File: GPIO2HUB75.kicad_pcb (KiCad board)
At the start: 2 copper layers, 33 x 57.1 mm, 3 parts, among them J1 Conn_02x10_Odd_Even, J2 Conn_02x20_Odd_Even_MountingP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, J3 Conn_02x08_Top_Bottom

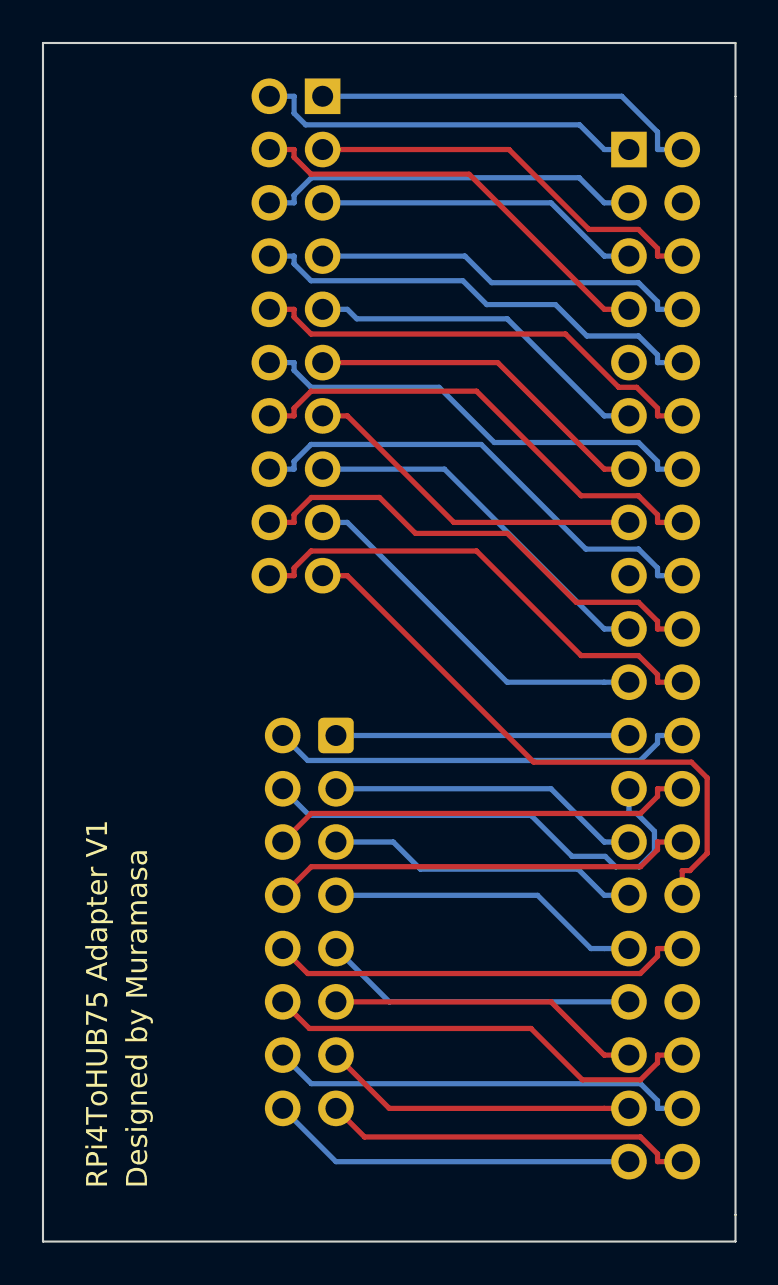
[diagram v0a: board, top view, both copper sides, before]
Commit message: added solder bridge to support 64x64+ panels
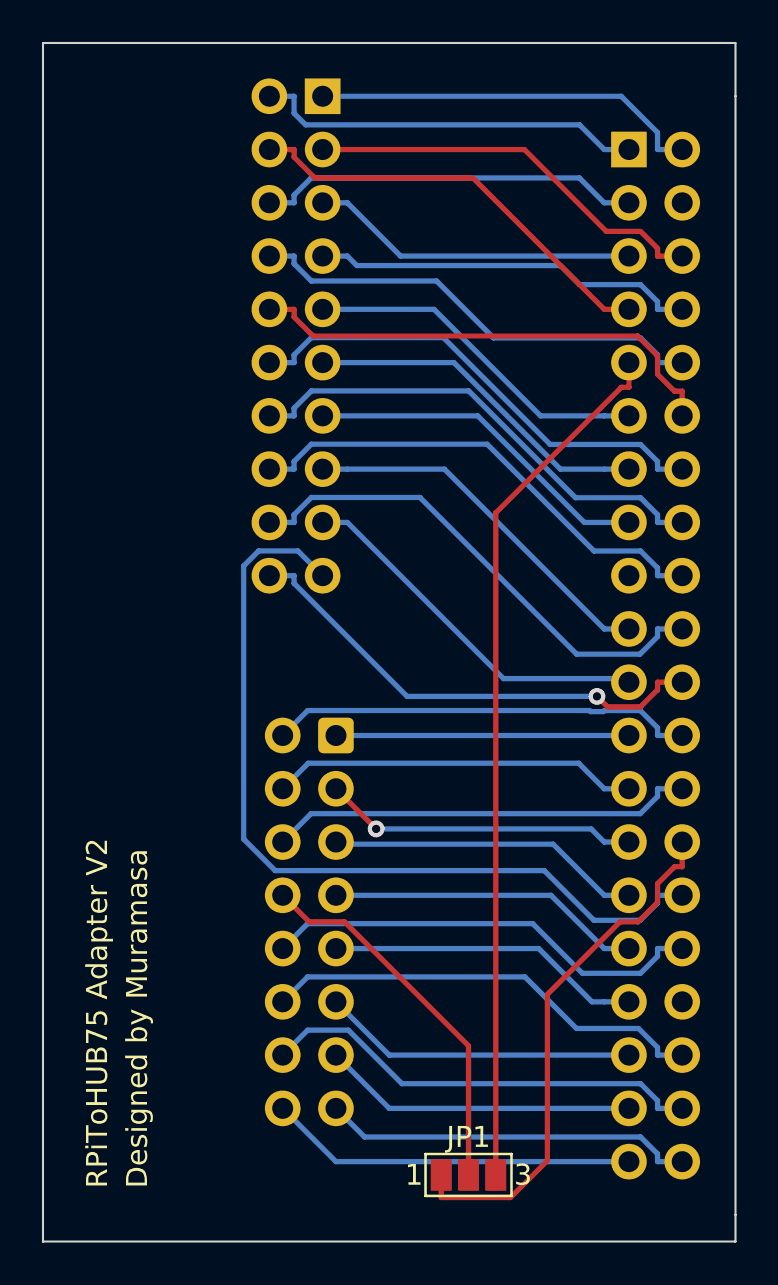
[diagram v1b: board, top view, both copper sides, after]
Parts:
- added JP1: SolderJumper_3_Open, Jumper:SolderJumper-3_P1.3mm_Open_Pad1.0x1.5mm_NumberLabels, F.Cu at (114.3, 102.2)
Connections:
- J2 pad 9: unconnected-(J2-Pin_9-Pad9) -> Net-(J2-Pin_9)
- J3 pad 8: Net-(J2-Pin_28) -> Net-(J3-Pin_8)
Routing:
- net Net-(J2-Pin_9): track 0.00 -> 41.6 mm
- net Net-(J3-Pin_8): track 0.00 -> 18.0 mm
- net Net-(J1-Pin_19): track 28.6 -> 40.8 mm
- net Net-(J2-Pin_25): track 23.3 -> 17.5 mm
- net Net-(J2-Pin_28): track 20.3 -> 25.4 mm
- net Net-(J1-Pin_18): track 23.2 -> 24.2 mm
- net Net-(J1-Pin_12): track 22.2 -> 23.2 mm
- net Net-(J2-Pin_38): track 20.3 -> 21.3 mm
- net Net-(J1-Pin_10): track 22.2 -> 23.2 mm
- net Net-(J2-Pin_32): track 20.3 -> 21.2 mm
- net Net-(J1-Pin_20): vias 0 -> 1
- net Net-(J2-Pin_27): vias 0 -> 1
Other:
- board text added: "RPiToHUB75 Adapter V2"
- board text removed: "RPi4ToHUB75 Adapter V1"

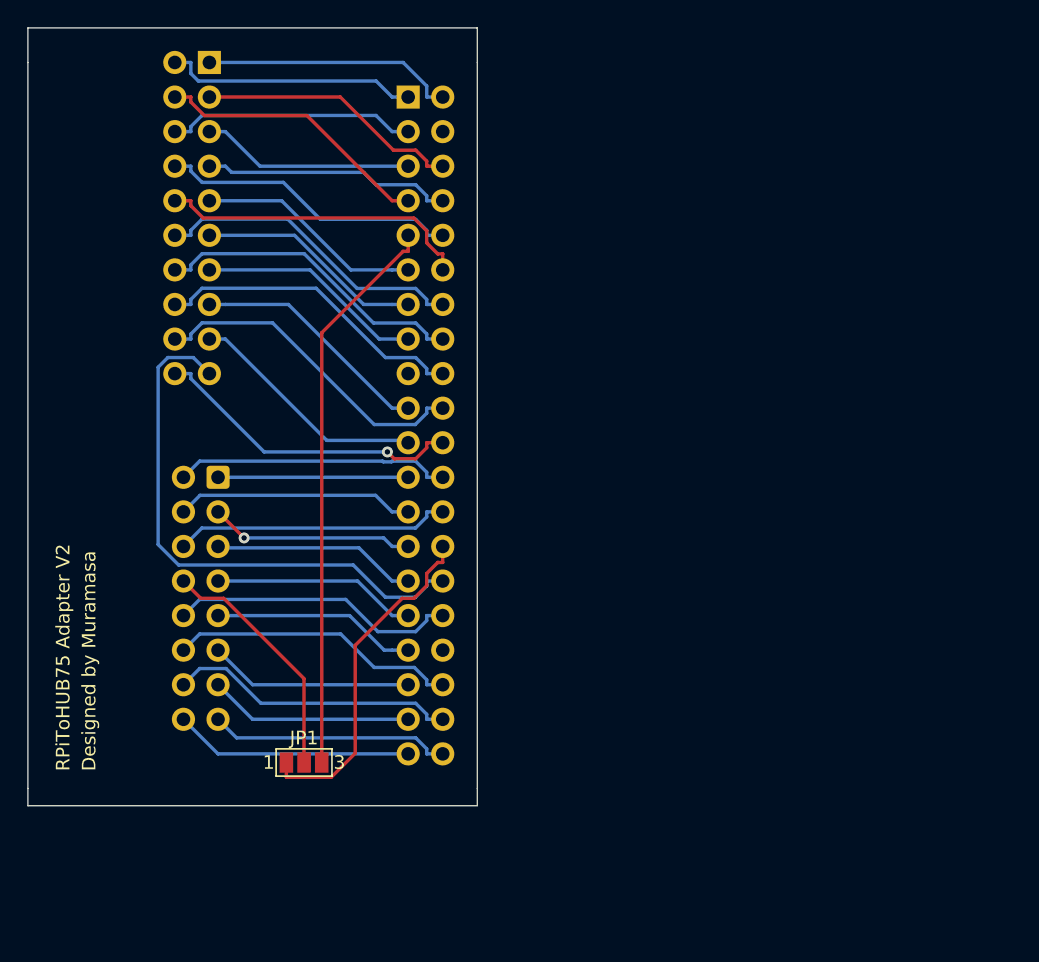
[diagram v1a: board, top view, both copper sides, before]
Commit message: added a 3pin fan header
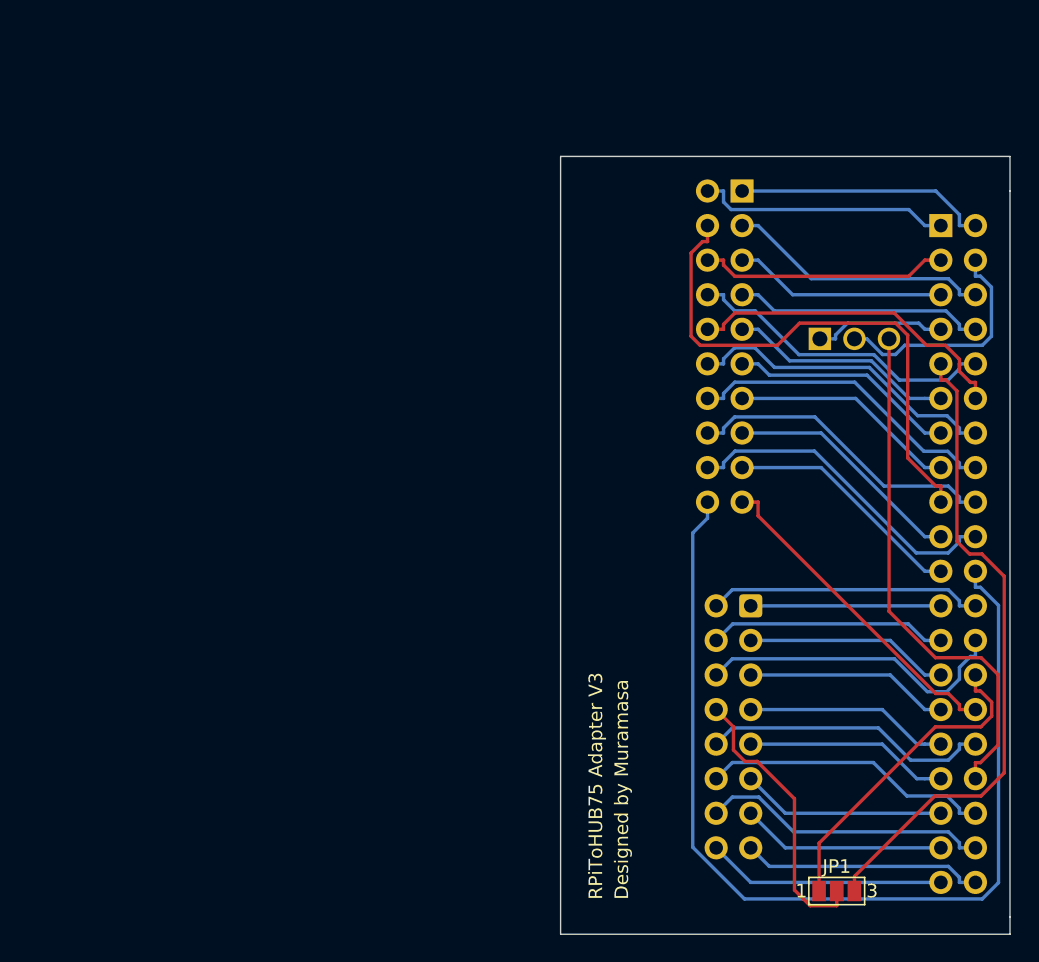
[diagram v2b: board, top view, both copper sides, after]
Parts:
- added M1: Fan_3pin, 3 Pin Fan Header Angled:HDRRA3W64P0X254_1X3_747X318X635P, B.Cu at (152.2, 71.1)
- moved J1 40.3 mm to (146.5, 60.2)
- moved J2 40.3 mm to (161.1, 62.8)
- moved J3 40.3 mm to (147.1, 90.7)
- moved JP1 40.3 mm to (153.4, 111.7)
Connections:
- J2 pad 17: unconnected-(J2-Pin_17-Pad17) -> Net-(J1-Pin_4)
- J2 pad 34: unconnected-(J2-Pin_34-Pad34) -> Net-(J2-Pin_34)
- J2 pad 4: unconnected-(J2-Pin_4-Pad4) -> Net-(J2-Pin_4)
- J2 pad 7: Net-(J1-Pin_4) -> Net-(J2-Pin_7)
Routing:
- net Net-(J1-Pin_20): track 23.2 -> 74.1 mm, vias 1 -> 0
- net Net-(J2-Pin_34): track 0.00 -> 38.5 mm
- net Net-(J1-Pin_4): track 20.5 -> 39.6 mm
- net Net-(J2-Pin_4): track 0.00 -> 17.4 mm
- net Net-(J1-Pin_19): track 40.8 -> 24.3 mm
- net Net-(J2-Pin_7): track 0.00 -> 9.72 mm
- net Net-(J2-Pin_9): track 41.6 -> 48.0 mm
- net Net-(J2-Pin_26): track 20.3 -> 23.3 mm
- net Net-(J3-Pin_8): track 18.0 -> 20.8 mm
- net Net-(J2-Pin_28): track 25.4 -> 23.8 mm
- net Net-(J1-Pin_10): track 23.2 -> 24.2 mm
- net Net-(J1-Pin_8): track 22.2 -> 23.2 mm
- net Net-(J2-Pin_27): vias 1 -> 0
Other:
- board text added: "RPiToHUB75 Adapter V3"
- board text removed: "RPiToHUB75 Adapter V2"

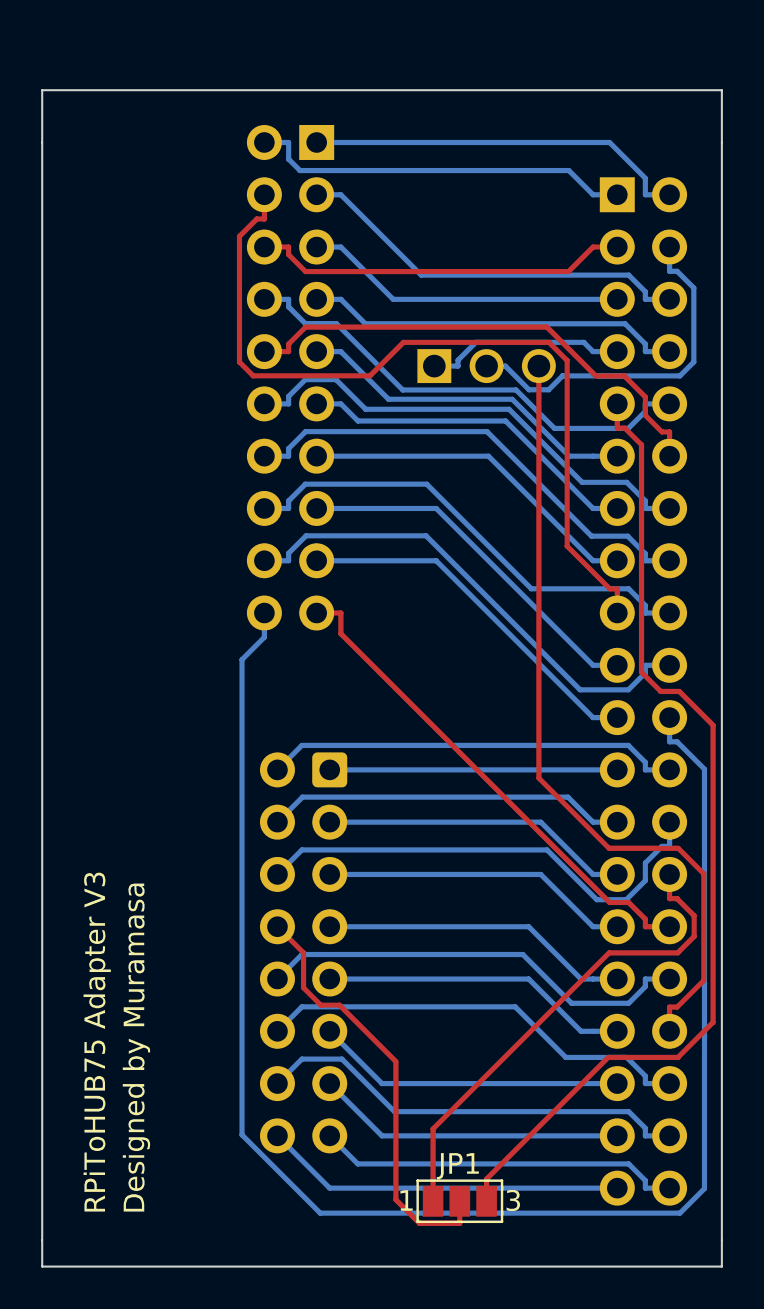
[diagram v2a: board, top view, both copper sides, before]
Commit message: added a buzzer and split input pins from general GPIO
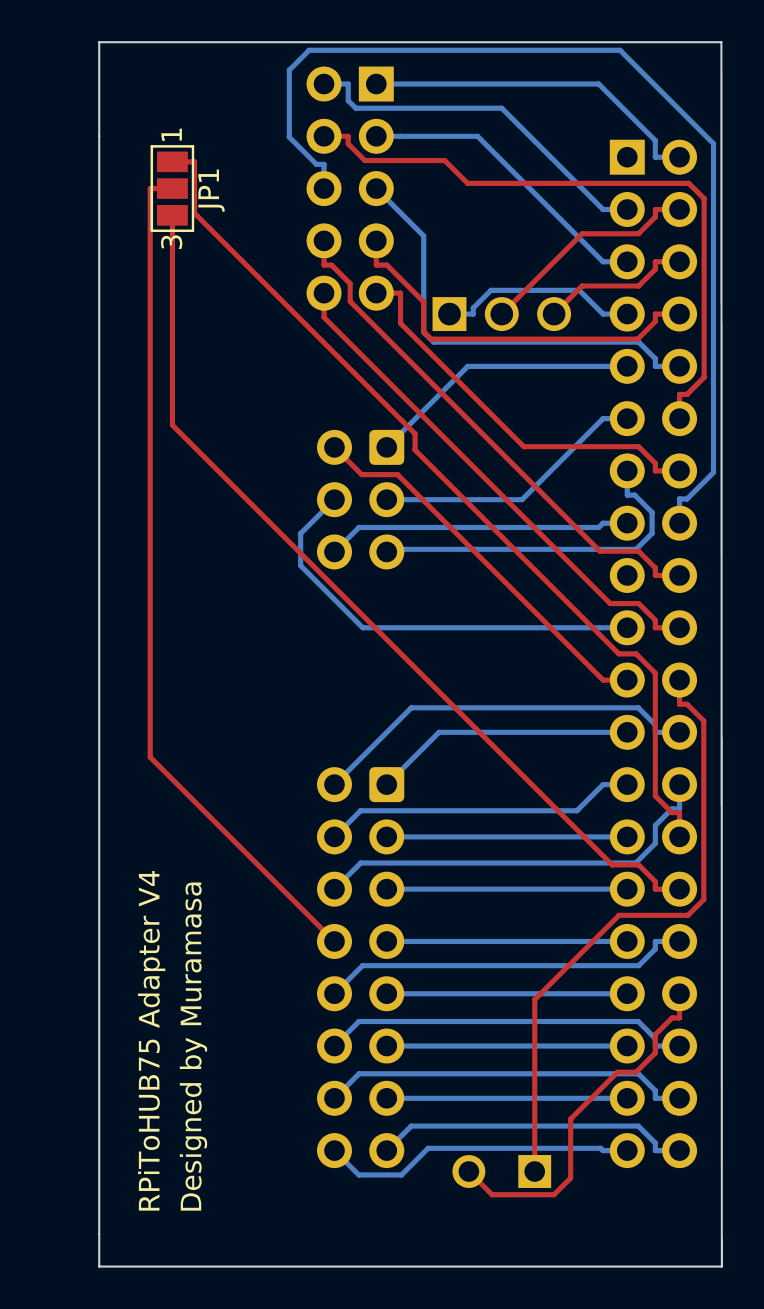
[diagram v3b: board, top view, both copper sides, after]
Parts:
- removed J1: Conn_02x10_Odd_Even, Connector_PinHeader_2.54mm:PinHeader_2x10_P2.54mm_Horizontal
- added BZ1: Buzzer, Buzzer_Beeper:MagneticBuzzer_Kingstate_KCG0601, B.Cu at (157.0, 110.2)
- added J4: Conn_02x05_Odd_Even, Connector_PinHeader_2.54mm:PinHeader_2x05_P2.54mm_Horizontal, B.Cu at (149.4, 57.4)
- added J5: Conn_02x03_Odd_Even, Connector_IDC:IDC-Header_2x03_P2.54mm_Horizontal, B.Cu at (149.9, 75.1)
- moved JP1 51.1 mm to (139.4, 62.5), turned to -90 degrees
- moved J3 2.86 mm to (149.9, 91.4)
- moved M1 2.63 mm to (152.9, 68.6)
- moved J2 1.89 mm to (161.5, 61.0)
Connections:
- J2 pad 1: Net-(J1-Pin_2) -> unconnected-(J2-Pin_1-Pad1)
- J2 pad 17: Net-(J1-Pin_4) -> unconnected-(J2-Pin_17-Pad17)
- J2 pad 30: Net-(J1-Pin_19) -> Net-(J2-Pin_30)
- J2 pad 34: Net-(J2-Pin_34) -> Net-(BZ1-+)
- J2 pad 6: Net-(J1-Pin_3) -> Net-(J2-Pin_6)
- JP1 pad 3: Net-(J2-Pin_9) -> Net-(J2-Pin_30)
- M1 pad 3: Net-(J2-Pin_34) -> Net-(J2-Pin_6)
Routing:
- net Net-(J2-Pin_30): track 0.00 -> 44.4 mm
- net Net-(BZ1--): track 74.1 -> 29.9 mm
- net Net-(J1-Pin_4): track 39.6 -> 0.00 mm
- net Net-(J2-Pin_34): track 38.5 -> 0.00 mm
- net Net-(J2-Pin_9): track 48.0 -> 13.3 mm
- net Net-(J2-Pin_16): track 23.2 -> 48.9 mm
- net Net-(J1-Pin_19): track 24.3 -> 0.00 mm
- net Net-(J2-Pin_28): track 23.8 -> 44.3 mm
- net Net-(J3-Pin_8): track 20.8 -> 41.4 mm
- net Net-(J1-Pin_3): track 19.5 -> 0.00 mm
- net Net-(J1-Pin_2): track 18.7 -> 0.00 mm
- net Net-(BZ1-+): track 0.00 -> 17.6 mm
- net Net-(J2-Pin_6): track 0.00 -> 7.36 mm
- net Net-(J2-Pin_12): track 24.2 -> 31.3 mm
- net Net-(J2-Pin_4): track 17.4 -> 11.0 mm
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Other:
- board size 33 x 57.1 mm -> 30.2 x 59.5 mm
- board text added: "RPiToHUB75 Adapter V4"
- board text removed: "RPiToHUB75 Adapter V3"
